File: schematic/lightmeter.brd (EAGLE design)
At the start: 27.9 x 52.1 mm, 77 parts, among them IC2 MCP73831/OT, J1 AVR_SPI_PRG_6NS, Q1 NCHANNELMOSFET, Q10 PCHANNELMOSFET, Q11 NCHANNELMOSFET, Q12 NCHANNELMOSFET, Q13 NCHANNELMOSFET, Q14 NCHANNELMOSFET, Q2 PCHANNELMOSFET, Q3 NCHANNELMOSFET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

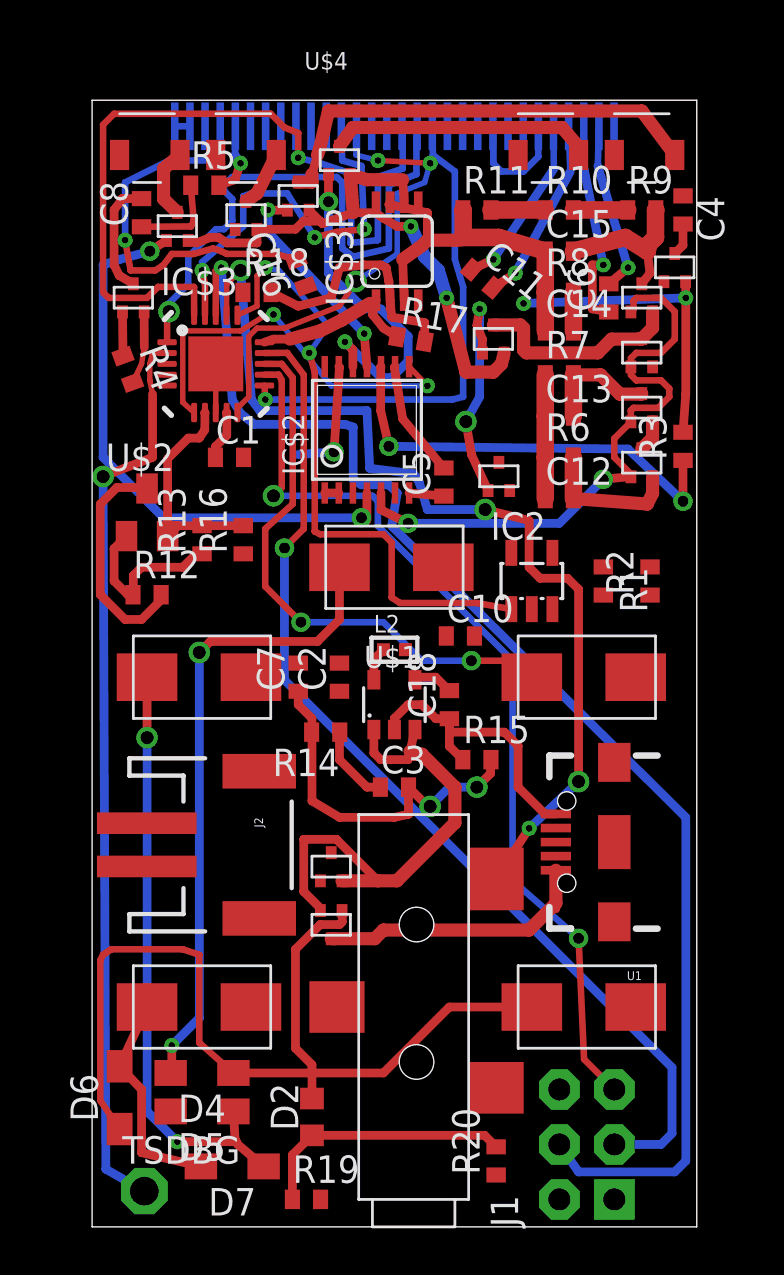
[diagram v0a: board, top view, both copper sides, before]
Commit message: More work on routing.
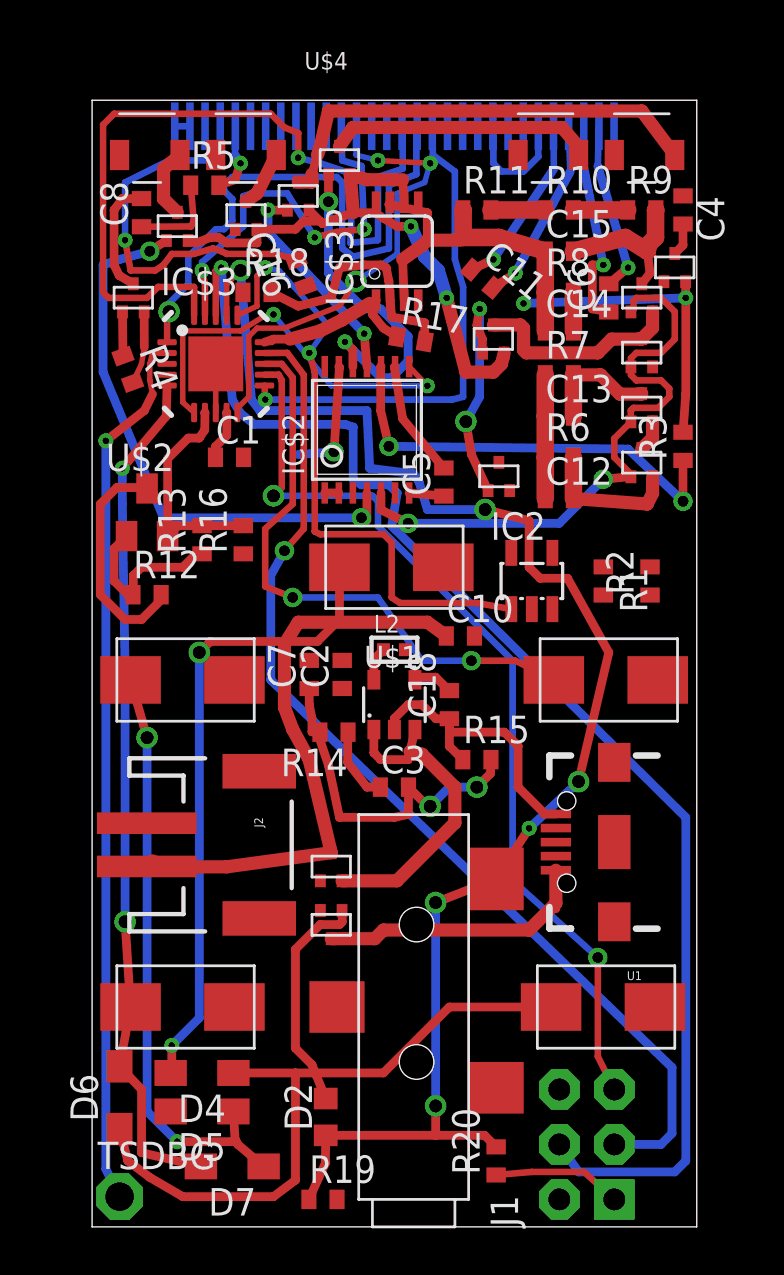
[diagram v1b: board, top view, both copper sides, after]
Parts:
- moved TSDBG 1.17 mm to (0.00, 1.40)
- moved S4 1.02 mm to (22.6, 25.3)
- moved S1 0.89 mm to (22.5, 10.2)
- moved S5 0.77 mm to (3.05, 25.3)
- moved R19 0.76 mm to (9.40, 1.27)
- moved S3 0.76 mm to (3.05, 10.2)
- moved D2 0.63 mm to (9.53, 5.08)
- moved C7 0.52 mm to (8.76, 25.5)
- moved R14 0.38 mm to (9.91, 22.9)
- moved C2 0.18 mm to (10.3, 25.5)
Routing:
- net PBI$2: track 10.2 -> 39.5 mm, vias 0 -> 2
- net VBAT: track 0.36 -> 27.0 mm
- net AVRMISO/FLASHSYNC: track 56.9 -> 76.2 mm, vias 4 -> 6
- net VCC: track 22.8 -> 15.1 mm
- net N$8: track 34.1 -> 30.9 mm
- net N$23: track 42.0 -> 40.8 mm
- net PBI$3: track 25.9 -> 27.0 mm
- net DIODESW$1: track 26.7 -> 26.1 mm
- net AVRSCK: track 48.0 -> 48.6 mm

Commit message: More work on routing.
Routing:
- net PBI$3: track 27.0 -> 62.8 mm, vias 2 -> 3
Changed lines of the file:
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@@
 <wire x1="4.94538125" y1="42.128" x2="4.953" y2="43.561" width="0.254" layer="1"/>
 <wire x1="4.953" y1="43.561" x2="5.588" y2="44.196" width="0.254" layer="1"/>
-<via x="5.588" y="44.196" extent="1-16" drill="0.6" shape="square"/>
+<via x="5.588" y="44.196" extent="1-16" drill="0.3" shape="square"/>
 <wire x1="5.588" y1="44.196" x2="6.096" y2="38.227" width="0.4064" layer="16"/>
 <wire x1="6.096" y1="38.227" x2="6.477" y2="37.719" width="0.4064" layer="16"/>
@@
 <wire x1="16.256" y1="26.162" x2="18.288" y2="26.162" width="0.3048" layer="1"/>
 <wire x1="18.288" y1="26.162" x2="20.066" y2="25.273" width="0.3048" layer="1"/>
-<wire x1="2.36" y1="5.334" x2="13.97" y2="26.162" width="0" layer="19" extent="1-16"/>
+<wire x1="2.36" y1="5.334" x2="3.81" y2="6.35" width="0.4064" layer="1"/>
+<wire x1="3.81" y1="6.35" x2="3.81" y2="8.255" width="0.4064" layer="1"/>
+<wire x1="3.81" y1="8.255" x2="4.191" y2="8.382" width="0.4064" layer="1"/>
+<wire x1="4.191" y1="8.382" x2="6.858" y2="8.382" width="0.4064" layer="1"/>
+<via x="6.858" y="8.382" extent="1-16" drill="0.6" shape="square"/>
+<wire x1="6.858" y1="8.382" x2="5.969" y2="12.954" width="0.4064" layer="16"/>
+<wire x1="5.969" y1="12.954" x2="5.969" y2="29.972" width="0.4064" layer="16"/>
+<wire x1="5.969" y1="29.972" x2="6.731" y2="30.734" width="0.4064" layer="16"/>
+<wire x1="6.731" y1="30.734" x2="6.731" y2="32.004" width="0.4064" layer="16"/>
+<wire x1="6.731" y1="32.004" x2="7.366" y2="32.131" width="0.4064" layer="16"/>
+<wire x1="7.366" y1="32.131" x2="8.636" y2="32.131" width="0.4064" layer="16"/>
+<wire x1="8.636" y1="32.131" x2="8.636" y2="30.734" width="0.4064" layer="16"/>
+<wire x1="8.636" y1="30.734" x2="8.001" y2="29.083" width="0.4064" layer="16"/>
 </signal>
 <signal name="PBI$1">
@@
 <wire x1="4.318" y1="49.276" x2="4.699" y2="49.53" width="0.3048" layer="16"/>
 <wire x1="4.699" y1="49.53" x2="4.65" y2="50.857" width="0.3048" layer="16"/>
-<wire x1="2.413" y1="44.958" x2="3.429" y2="44.958" width="0.3048" layer="1"/>
-<wire x1="3.429" y1="44.958" x2="4.318" y2="45.212" width="0.3048" layer="1"/>
-<wire x1="4.318" y1="45.212" x2="4.699" y2="45.085" width="0.3048" layer="1"/>
-<wire x1="4.699" y1="45.085" x2="4.953" y2="44.958" width="0.3048" layer="1"/>
-<wire x1="4.953" y1="44.958" x2="7.239" y2="44.958" width="0.3048" layer="1"/>
+<wire x1="2.413" y1="44.958" x2="7.239" y2="44.958" width="0.3048" layer="1"/>
 </signal>
 <signal name="N$23">

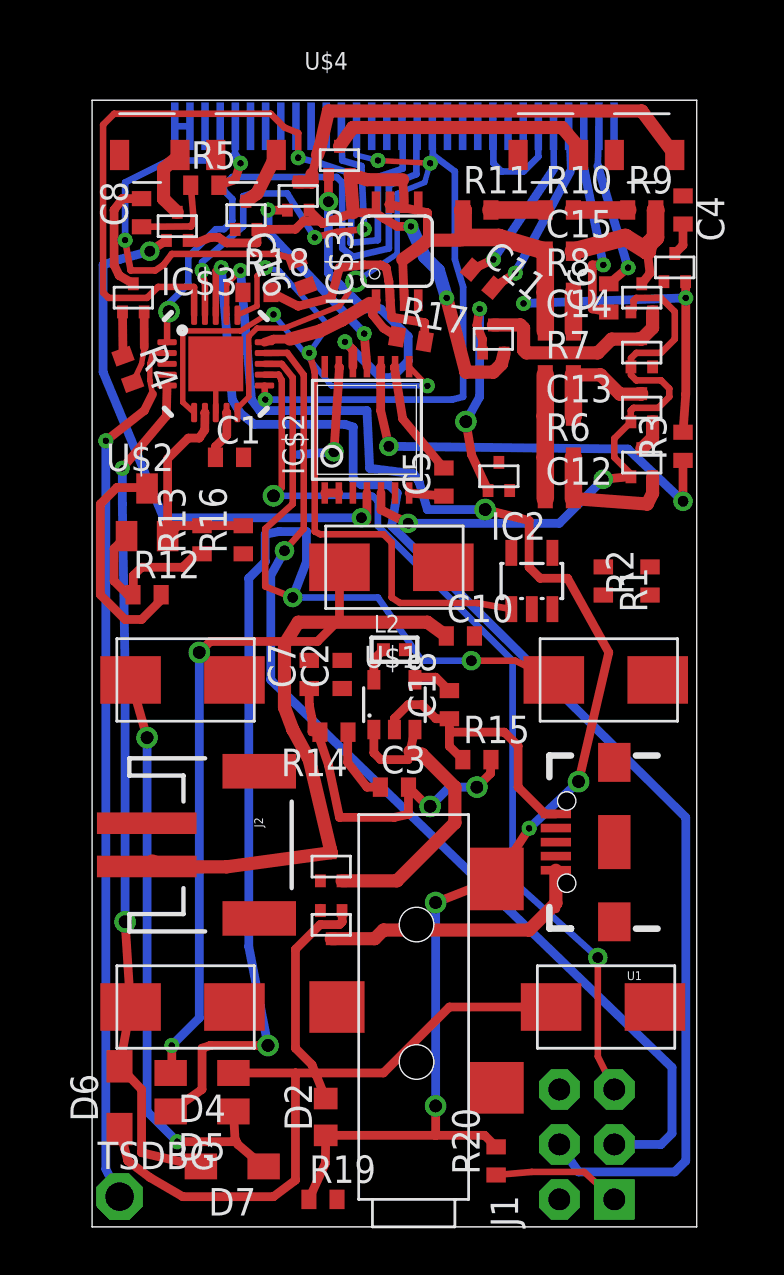
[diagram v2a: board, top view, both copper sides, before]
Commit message: More work on routing.
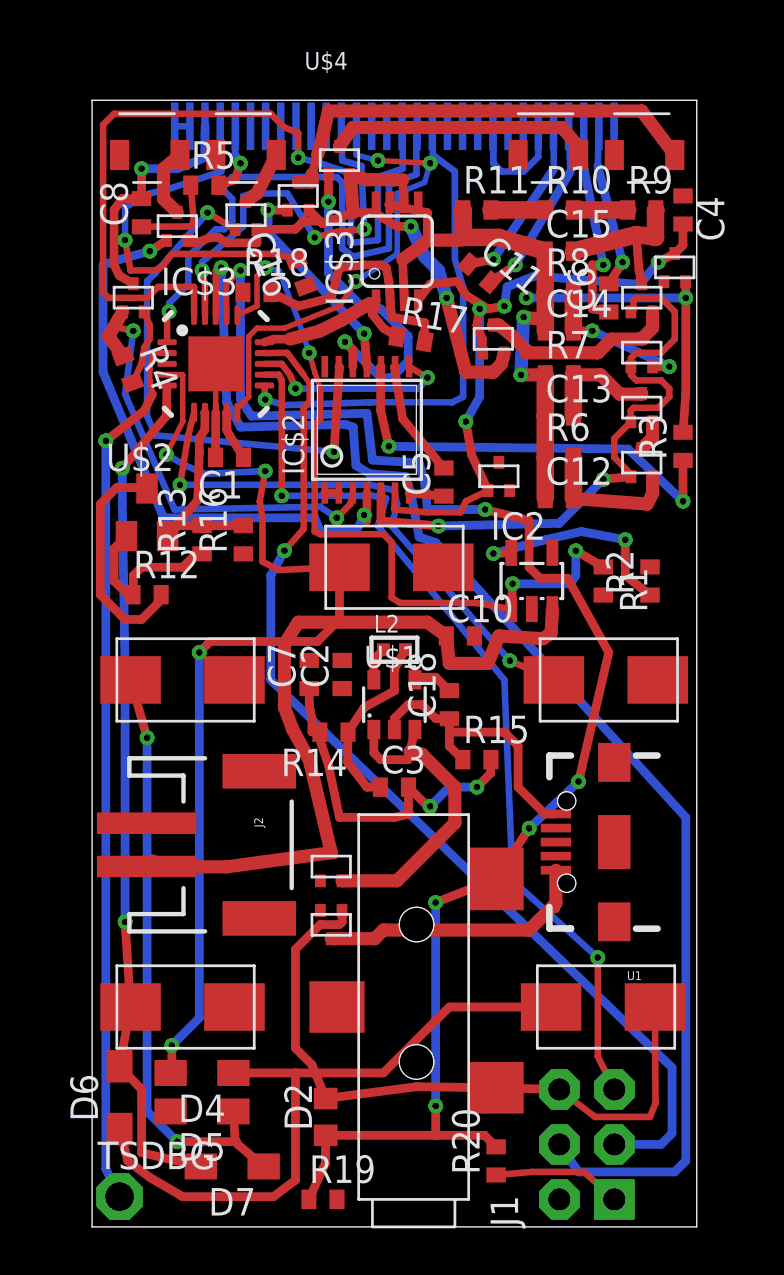
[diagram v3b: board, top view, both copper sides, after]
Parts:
- moved C11 0.28 mm to (16.6, 44.1)
- turned C1 to 180 degrees
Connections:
- net PBI$3: now also IC$3.6; no longer IC$3.13
- net SRCLK: now also IC$3.13; no longer IC$3.6
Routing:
- net PBI$3: track 62.8 -> 25.5 mm, vias 3 -> 2
- net GND: track 57.7 -> 80.2 mm
- net DIODESW$2: track 5.61 -> 25.2 mm, vias 1 -> 2
- net SCRPWR: track 2.05 -> 21.2 mm, vias 0 -> 2
- net PBI$1: track 29.5 -> 46.8 mm, vias 2 -> 4
- net N$6: track 1.52 -> 15.7 mm, vias 0 -> 2
- net N$5: track 0.00 -> 10.2 mm, vias 0 -> 2
- net SRCLK: track 18.3 -> 9.45 mm
- net VBAT: track 27.0 -> 35.0 mm
- net BATSTAT: track 28.8 -> 34.9 mm, vias 2 -> 4
- net SCRVREG: track 11.0 -> 16.9 mm, vias 0 -> 1
- net N$3: track 1.78 -> 7.34 mm, vias 0 -> 2
- net STG$2: track 10.9 -> 16.4 mm
- net N$17: track 3.47 -> 8.46 mm
- net OAOUT1: track 22.8 -> 27.6 mm, vias 0 -> 2
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
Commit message: Add battery voltage input; more work on board
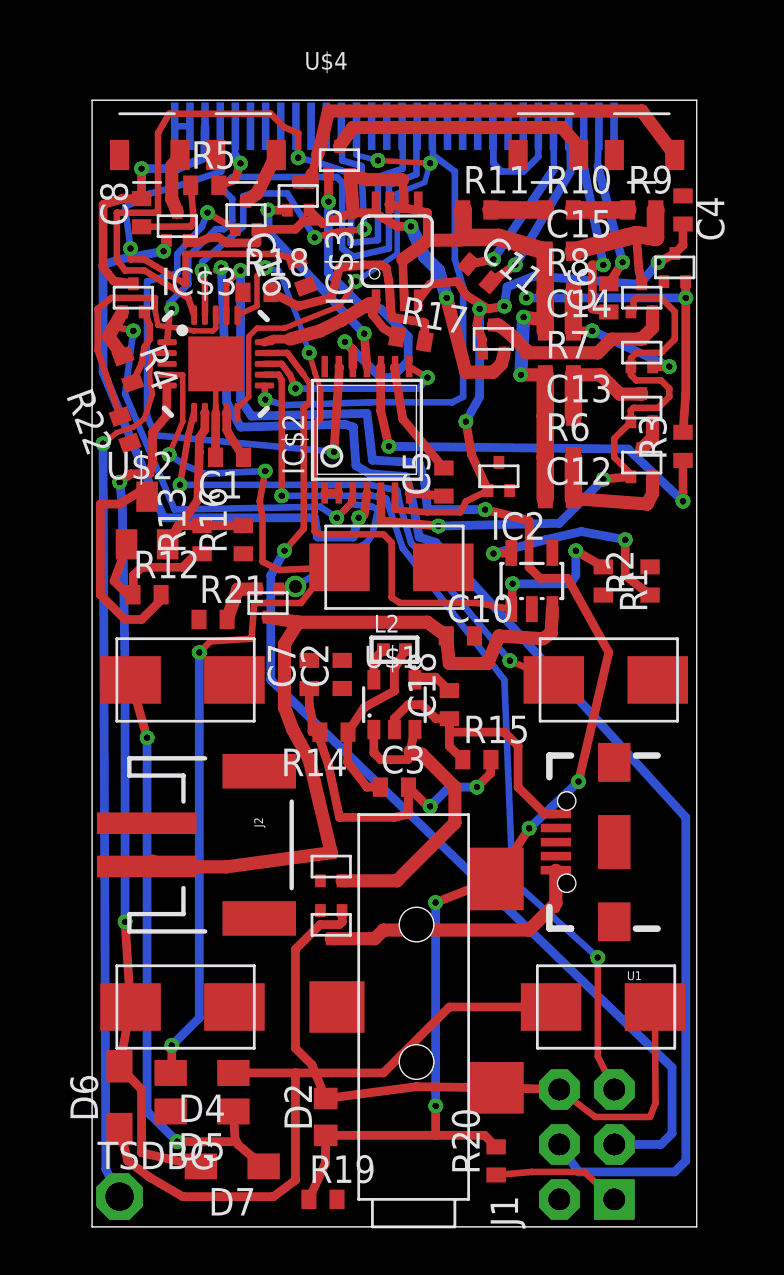
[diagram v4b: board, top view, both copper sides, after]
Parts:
- added Q16: NCHANNELMOSFET, lightmeter:SOT-416-3
- added R21: 10K, resistor:R0402
- added R22: 2.2K, resistor:R0402
- moved U$2 0.38 mm to (1.27, 32.6)
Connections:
- new net AVRMOSI/BATVOLTAGE: IC$3.18, R21.1, R22.2
- new net N$30: Q16.P$2, R21.2
- net AVRMOSI: no longer IC$3.18
- net GND: now also R22.1
- net SCRPWR: now also Q16.P$1
- net VBAT: now also Q16.P$3
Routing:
- net AVRMOSI/BATVOLTAGE: track 0.00 -> 12.6 mm
- net SCRPWR: track 21.2 -> 29.6 mm, vias 2 -> 3
- net SCRDC: track 37.5 -> 34.2 mm
- net N$30: track 0.00 -> 2.38 mm
- net AVRMOSI: track 62.7 -> 60.7 mm
- net VBAT: track 35.0 -> 36.4 mm
- net PBI$1: track 46.8 -> 45.6 mm
- net SCRVREG: track 16.9 -> 18.0 mm
- net N$12: track 17.8 -> 18.7 mm
- net PBI$2: track 39.5 -> 40.1 mm
- net VREF: track 10.00 -> 10.6 mm
- net N$25: track 7.93 -> 7.41 mm

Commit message: More work on layout.
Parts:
- moved C4 10.9 mm to (15.5, 49.8), turned to 0 degrees
- moved C10 0.68 mm to (15.5, 26.7)
- moved IC2 0.25 mm to (19.3, 29.8)
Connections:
- net GND: now also C4.2
- net N$6: no longer C4.2
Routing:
- net VREG: track 29.6 -> 64.1 mm, vias 2 -> 4
- net GND: track 80.5 -> 107.9 mm
- net VUSB: track 14.4 -> 33.5 mm
- net SCRDC: track 34.2 -> 31.0 mm
- net OAOUT1: track 27.6 -> 30.1 mm
- net N$26: track 27.2 -> 24.9 mm
- net SCRCLK: track 21.8 -> 23.4 mm
- net BATSTAT: track 34.9 -> 36.3 mm
- net N$6: track 15.7 -> 14.7 mm
- net SCRCS: track 23.0 -> 23.7 mm

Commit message: More work on layout.
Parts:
- moved R4 17.4 mm to (17.7, 37.5)
- moved R2 0.89 mm to (25.4, 29.8)
- moved R17 0.63 mm to (14.1, 41.0)
- moved C16 0.57 mm to (8.13, 44.6)
- moved C4 0.51 mm to (16.0, 49.8)
- moved Q6 0.25 mm to (17.8, 34.9)
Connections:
- net N$22: now also Q6.P$2
- net N$26: now also Q6.P$3
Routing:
- net VREG: track 64.1 -> 113.0 mm, vias 4 -> 11
- net GND: track 107.9 -> 92.9 mm
- net SCRPWR: track 29.6 -> 42.2 mm
- net N$22: track 1.45 -> 13.1 mm
- net VUSB: track 33.5 -> 41.0 mm
- net STG$2: track 16.4 -> 23.2 mm, vias 2 -> 4
- net SCRCLK: track 23.4 -> 28.2 mm
- net DIODESW$3: track 15.8 -> 12.2 mm
- net SCRDC: track 31.0 -> 28.3 mm
- net N$12: track 18.7 -> 17.1 mm
- net STG$1: track 29.4 -> 30.7 mm
- net N$5: track 10.0 -> 11.2 mm
- net DIODESW$4: track 9.92 -> 10.8 mm
- net DIODESW$2: track 25.7 -> 24.8 mm
- net PBI$1: track 45.5 -> 46.3 mm
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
